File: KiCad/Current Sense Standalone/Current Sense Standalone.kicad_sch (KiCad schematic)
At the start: 11 parts, among them J1 PLUG INPUT BATTERY IN HERE (X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, J3 V+/- TEST Header PIN, J4 BAT +TERMINAL TEST HEADER PIN, J5 HEADER PIN FOR TEST, J6 to MCU GPIO PIN, J7 PLUG BATTERY OUTPUT HERE (XT6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, U1 INA139QPWRQ1

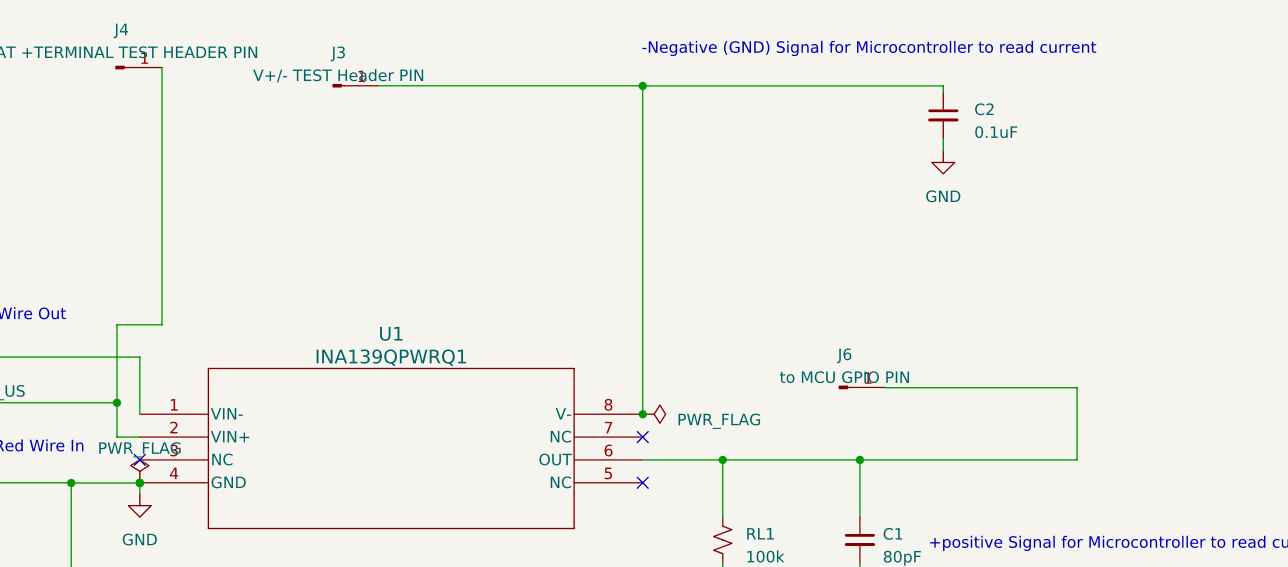
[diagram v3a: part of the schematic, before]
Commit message: Current Sense Update
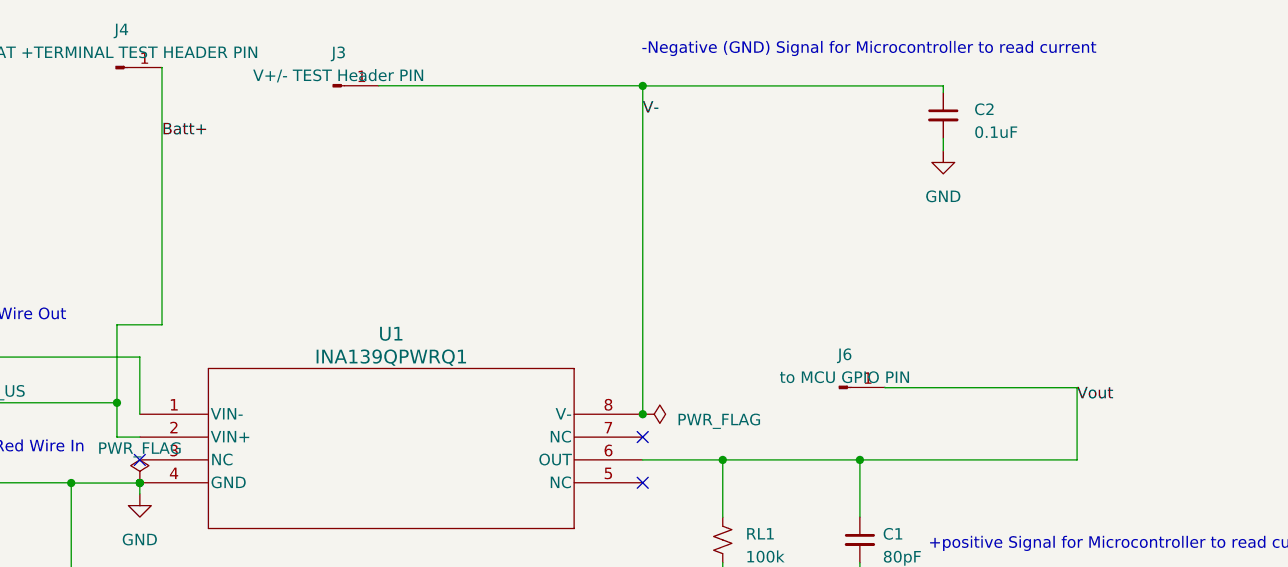
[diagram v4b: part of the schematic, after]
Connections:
- net V-: now reaches C2.1, J3.1 (Pin_1), U1.8 (V-)
- net Vout: now reaches C1.1, J6.1 (Pin_1), RL1.1, U1.6 (OUT)
- net Batt+: now reaches J1.1 (Pin_1), J4.1 (Pin_1), Rs1.2, U1.2 (VIN+)
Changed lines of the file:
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@@
+    (effects (font (size 1.27 1.27)) (justify left bottom))
+  )
+  (label "Vout" (at 250.19 85.09 0) (fields_autoplaced)
+    (effects (font (size 1.27 1.27)) (justify left bottom))
+  )
+  (label "Batt+" (at 148.5138 55.755 0) (fields_autoplaced)
+    (effects (font (size 1.27 1.27)) (justify left bottom))
+  )
+  (label "V-" (at 201.93 53.34 0) (fields_autoplaced)
     (effects (font (size 1.27 1.27)) (justify left bottom))
   )

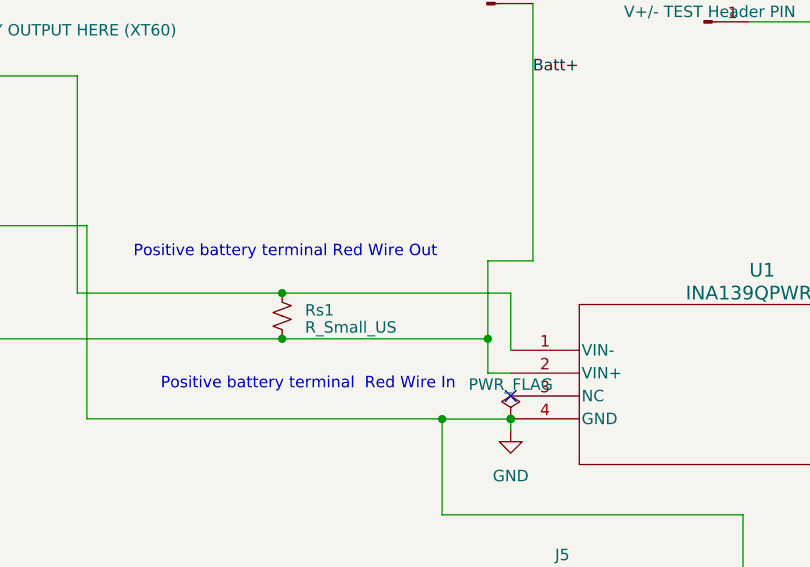
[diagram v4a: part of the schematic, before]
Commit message: Current Sense Update
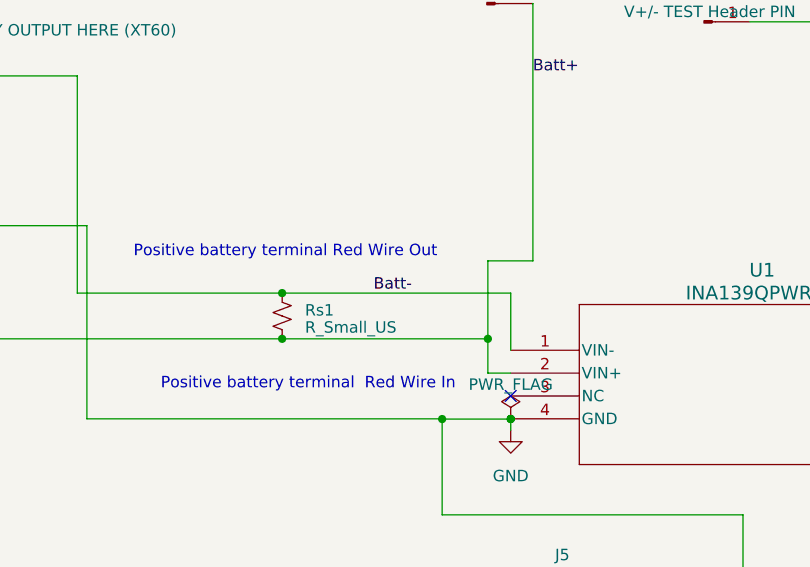
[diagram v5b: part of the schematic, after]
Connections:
- net Batt-: now reaches J7.1 (Pin_1), Rs1.1, U1.1 (VIN-)
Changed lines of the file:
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@@
+    (effects (font (size 1.27 1.27)) (justify left bottom))
+  )
+  (label "Batt-" (at 130.81 80.01 0) (fields_autoplaced)
     (effects (font (size 1.27 1.27)) (justify left bottom))
   )

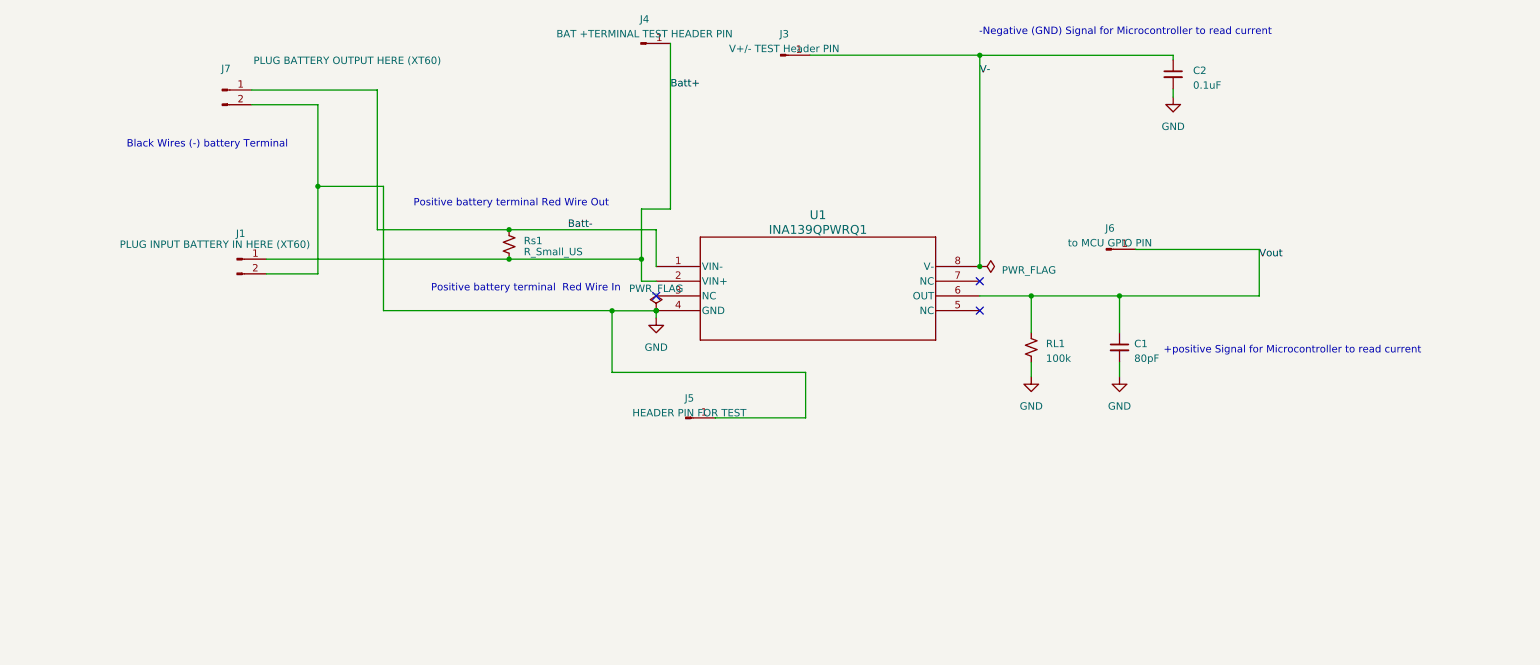
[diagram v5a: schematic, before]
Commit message: Updated Current Sense Standalone
new footprint for R_SENSE and fixed header pins
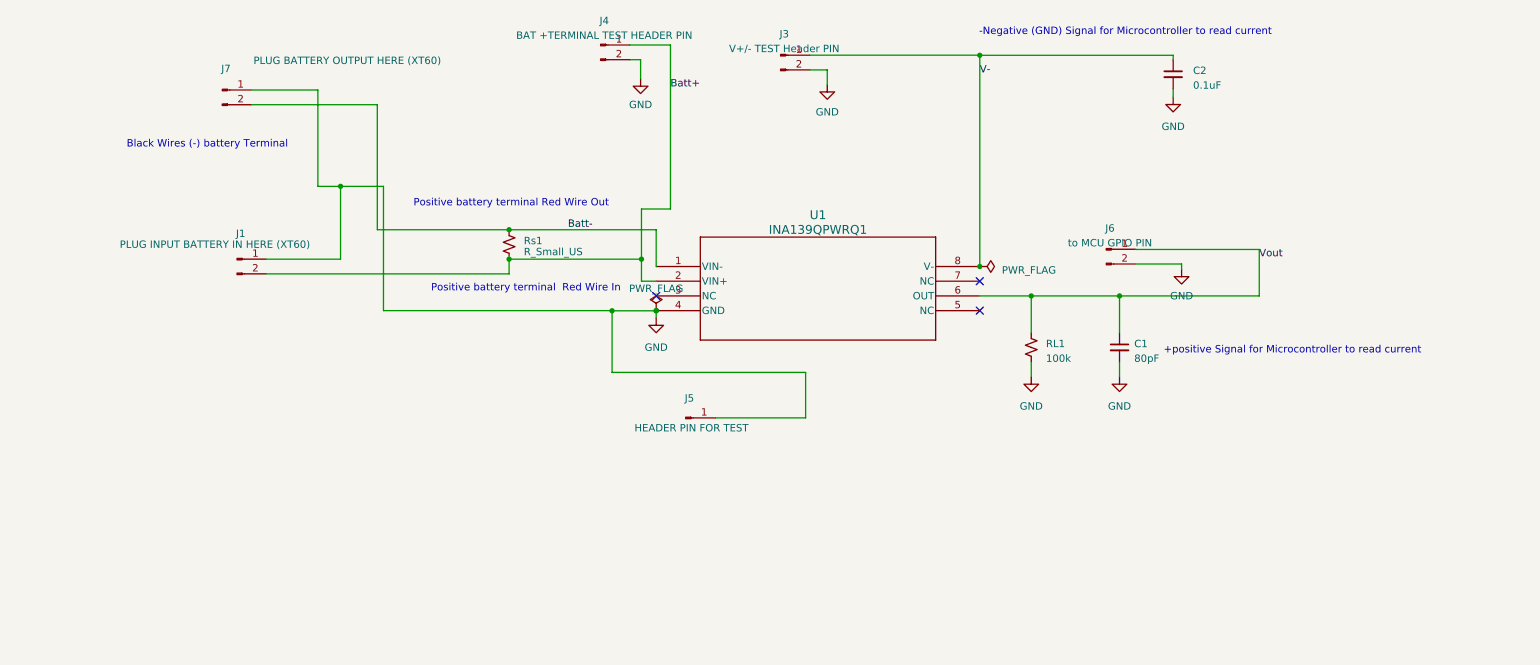
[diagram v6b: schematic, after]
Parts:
- J3, J4, J6: symbol Connector:Conn_01x01_Pin -> Connector:Conn_01x02_Pin
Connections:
- net Batt+: now also J1.2 (Pin_2); no longer J1.1 (Pin_1)
- net Batt-: now also J7.2 (Pin_2); no longer J7.1 (Pin_1)
- net GND: now also J1.1 (Pin_1), J3.2 (Pin_2), J4.2 (Pin_2), J6.2 (Pin_2), J7.1 (Pin_1); no longer J1.2 (Pin_2), J7.2 (Pin_2)
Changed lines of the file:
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@@
   (junction (at 120.65 80.01) (diameter 0) (color 0 0 0 0)
   )
-  (junction (at 120.65 85.09) (diameter 0) (color 0 0 0 0)
-  )
-  (junction (at 87.63 72.517) (diameter 0) (color 0 0 0 0)
-  )
   (junction (at 146.05 94.006) (diameter 0) (color 0 0 0 0)
   )
@@
   (junction (at 226.06 91.44) (diameter 0) (color 0 0 0 0)
   )
+  (junction (at 91.5454 72.517) (diameter 0) (color 0 0 0 0)
+  )
   (junction (at 201.93 86.36) (diameter 0) (color 0 0 0 0)
   )
+  (junction (at 120.65 85.09) (diameter 0) (color 0 0 0 0)
+  )
   (junction (at 210.82 91.44) (diameter 0) (color 0 0 0 0)
   )
@@
   (no_connect (at 201.93 88.9))
   (no_connect (at 201.93 93.98))
-  (wire (pts (xy 78.74 87.63) (xy 87.63 87.63))
-    (stroke (width 0) (type default))
-  )
   (wire (pts (xy 146.05 80.01) (xy 146.05 86.36))
     (stroke (width 0) (type default))
@@
     (stroke (width 0) (type default))
   )
-  (wire (pts (xy 87.63 72.517) (xy 87.63 87.63))
-    (stroke (width 0) (type default))
-  )
   (wire (pts (xy 138.43 93.98) (xy 138.43 94.006))
     (stroke (width 0) (type default))
@@
     (stroke (width 0) (type default))
   )
-  (wire (pts (xy 97.8916 80.01) (xy 97.8916 55.88))
-    (stroke (width 0) (type default))
-  )
-  (wire (pts (xy 87.63 58.42) (xy 87.63 72.517))
-    (stroke (width 0) (type default))
-  )
   (wire (pts (xy 156.2293 112.505) (xy 156.2293 112.4966))
     (stroke (width 0) (type default))
@@
     (stroke (width 0) (type default))
   )
-  (wire (pts (xy 87.63 72.517) (xy 98.9584 72.517))
-    (stroke (width 0) (type default))
-  )
   (wire (pts (xy 156.2293 112.4966) (xy 171.8564 112.4966))
     (stroke (width 0) (type default))
@@
     (stroke (width 0) (type default))
   )
-  (wire (pts (xy 97.8916 55.88) (xy 76.2 55.88))
+  (wire (pts (xy 201.93 49.8856) (xy 235.3257 49.8856))
     (stroke (width 0) (type default))
   )
-  (wire (pts (xy 201.93 49.8856) (xy 235.3257 49.8856))
+  (wire (pts (xy 78.74 85.09) (xy 91.5454 85.09))
+    (stroke (width 0) (type default))
+  )
+  (wire (pts (xy 76.2 55.88) (xy 87.63 55.88))
     (stroke (width 0) (type default))
   )
@@
     (stroke (width 0) (type default))
   )
+  (wire (pts (xy 236.7788 85.9252) (xy 236.7788 86.8426))
+    (stroke (width 0) (type default))
+  )
+  (wire (pts (xy 141.5288 50.6476) (xy 143.3576 50.6476))
+    (stroke (width 0) (type default))
+  )
   (wire (pts (xy 146.05 95.25) (xy 146.05 94.006))
     (stroke (width 0) (type default))
@@
     (stroke (width 0) (type default))
   )
-  (wire (pts (xy 76.2 58.42) (xy 87.63 58.42))
+  (wire (pts (xy 91.5454 72.517) (xy 98.9584 72.517))
+    (stroke (width 0) (type default))
+  )
+  (wire (pts (xy 87.63 55.88) (xy 87.63 72.517))
+    (stroke (width 0) (type default))
+  )
+  (wire (pts (xy 228.8553 85.9252) (xy 236.7788 85.9252))
+    (stroke (width 0) (type default))
+  )
+  (wire (pts (xy 120.65 87.63) (xy 120.65 85.09))
+    (stroke (width 0) (type default))
+  )
+  (wire (pts (xy 143.3576 50.6476) (xy 143.3576 53.9496))
     (stroke (width 0) (type default))
   )
-  (wire (pts (xy 78.74 85.09) (xy 120.65 85.09))
+  (wire (pts (xy 87.63 72.517) (xy 91.5454 72.517))
     (stroke (width 0) (type default))
   )
@@
     (stroke (width 0) (type default))
   )
-  (wire (pts (xy 148.5138 76.4286) (xy 148.5138 47.842))
+  (wire (pts (xy 148.5138 76.4286) (xy 148.5138 48.1076))
     (stroke (width 0) (type default))
   )
@@
     (stroke (width 0) (type default))
   )
+  (wire (pts (xy 91.5454 85.09) (xy 91.5454 72.517))
+    (stroke (width 0) (type default))
+  )
   (wire (pts (xy 201.93 91.44) (xy 210.82 91.44))
     (stroke (width 0) (type default))
   )
-  (wire (pts (xy 148.5138 47.842) (xy 148.4828 47.842))
+  (wire (pts (xy 148.5138 48.1076) (xy 141.5288 48.1076))
     (stroke (width 0) (type default))
   )
@@
     (stroke (width 0) (type default))
   )
+  (wire (pts (xy 175.5902 52.4073) (xy 175.5902 54.9402))
+    (stroke (width 0) (type default))
+  )
   (wire (pts (xy 210.82 91.44) (xy 226.06 91.44))
     (stroke (width 0) (type default))
@@
     (stroke (width 0) (type default))
   )
+  (wire (pts (xy 97.8916 58.42) (xy 97.8916 80.01))
+    (stroke (width 0) (type default))
+  )
   (wire (pts (xy 143.51 85.09) (xy 143.51 88.9))
     (stroke (width 0) (type default))
@@
     (stroke (width 0) (type default))
   )
+  (wire (pts (xy 78.74 87.63) (xy 120.65 87.63))
+    (stroke (width 0) (type default))
+  )
+  (wire (pts (xy 76.2 58.42) (xy 97.8916 58.42))
+    (stroke (width 0) (type default))
+  )
   (wire (pts (xy 148.5138 76.4286) (xy 143.51 76.4286))
     (stroke (width 0) (type default))
@@
     (stroke (width 0) (type default))
   )
+  (wire (pts (xy 172.6111 52.4073) (xy 175.5902 52.4073))
+    (stroke (width 0) (type default))
+  )
   (wire (pts (xy 235.3257 50.6164) (xy 235.3257 49.8856))
     (stroke (width 0) (type default))
@@
     (effects (font (size 1.27 1.27)) (justify left bottom))
   )
-  (symbol (lib_id "Connector:Conn_01x01_Pin") (at 167.5311 49.8673 0) (unit 1)
+  (symbol (lib_id "Connector:Conn_01x02_Pin") (at 167.5311 49.8673 0) (unit 1)
     (in_bom yes) (on_board yes) (dnp no) (fields_autoplaced)
     (property "Reference" "J3" (at 168.1661 46.2097 0)
@@
     )
     (pin "1")
+    (pin "2")
     (instances
       (project "Current Sense Standalone"
@@
     )
   )
-  (symbol (lib_id "Connector:Conn_01x01_Pin") (at 223.7753 83.3852 0) (unit 1)
+  (symbol (lib_id "Connector:Conn_01x02_Pin") (at 223.7753 83.3852 0) (unit 1)
     (in_bom yes) (on_board yes) (dnp no) (fields_autoplaced)
     (property "Reference" "J6" (at 224.4103 79.753 0)
@@
     )
     (pin "1")
+    (pin "2")
     (instances
       (project "Current Sense Standalone"
@@
     )
   )
+  (symbol (lib_id "power:GND") (at 175.5902 54.9402 0) (unit 1)
+    (in_bom yes) (on_board yes) (dnp no) (fields_autoplaced)
+    (property "Reference" "#PWR06" (at 175.5902 61.2902 0)
+      (effects (font (size 1.27 1.27)) hide)
+    )
+    (property "Value" "GND" (at 175.5902 59.69 0)
+      (effects (font (size 1.27 1.27)))
+    )
+    (property "Footprint" "" (at 175.5902 54.9402 0)
+      (effects (font (size 1.27 1.27)) hide)
+    )
+    (property "Datasheet" "" (at 175.5902 54.9402 0)
+      (effects (font (size 1.27 1.27)) hide)
+    )
+    (pin "1")
+    (instances
+      (project "Current Sense Standalone"
+        (path "/af3dddb2-191c-40a1-9395-0fad50eefcf8"
+          (reference "#PWR06") (unit 1)
+        )
+      )
+    )
+  )
   (symbol (lib_id "power:GND") (at 146.05 95.25 0) (unit 1)
     (in_bom yes) (on_board yes) (dnp no) (fields_autoplaced)
@@
   )
   (symbol (lib_id "Connector:Conn_01x01_Pin") (at 151.1493 112.505 0) (unit 1)
-    (in_bom yes) (on_board yes) (dnp no) (fields_autoplaced)
+    (in_bom yes) (on_board yes) (dnp no)
     (property "Reference" "J5" (at 151.7843 109.1014 0)
       (effects (font (size 1.27 1.27)))
     )
-    (property "Value" "HEADER PIN FOR TEST" (at 151.7843 111.6414 0)
+    (property "Value" "HEADER PIN FOR TEST" (at 152.146 114.2492 0)
       (effects (font (size 1.27 1.27)))
     )
@@
     )
   )
-  (symbol (lib_id "Connector:Conn_01x01_Pin") (at 143.4028 47.842 0) (unit 1)
+  (symbol (lib_id "Connector:Conn_01x02_Pin") (at 136.4488 48.1076 0) (unit 1)
     (in_bom yes) (on_board yes) (dnp no) (fields_autoplaced)
-    (property "Reference" "J4" (at 144.0378 43.651 0)
+    (property "Reference" "J4" (at 137.0838 43.9166 0)
       (effects (font (size 1.27 1.27)))
     )
-    (property "Value" "BAT +TERMINAL TEST HEADER PIN" (at 144.0378 46.191 0)
+    (property "Value" "BAT +TERMINAL TEST HEADER PIN" (at 137.0838 46.4566 0)
       (effects (font (size 1.27 1.27)))
     )
-    (property "Footprint" "Connector_PinHeader_2.54mm:PinHeader_1x02_P2.54mm_Vertical" (at 143.4028 47.842 0)
+    (property "Footprint" "Connector_PinHeader_2.54mm:PinHeader_1x02_P2.54mm_Vertical" (at 136.4488 48.1076 0)
       (effects (font (size 1.27 1.27)) hide)
     )
-    (property "Datasheet" "~" (at 143.4028 47.842 0)
+    (property "Datasheet" "~" (at 136.4488 48.1076 0)
       (effects (font (size 1.27 1.27)) hide)
     )
     (pin "1")
+    (pin "2")
     (instances
       (project "Current Sense Standalone"
@@
         )
       )
+    )
+  )
+  (symbol (lib_id "power:GND") (at 236.7788 86.8426 0) (unit 1)
+    (in_bom yes) (on_board yes) (dnp no) (fields_autoplaced)
+    (property "Reference" "#PWR07" (at 236.7788 93.1926 0)
+      (effects (font (size 1.27 1.27)) hide)
+    )
+    (property "Value" "GND" (at 236.7788 91.44 0)
+      (effects (font (size 1.27 1.27)))
+    )
+    (property "Footprint" "" (at 236.7788 86.8426 0)
+      (effects (font (size 1.27 1.27)) hide)
+    )
+    (property "Datasheet" "" (at 236.7788 86.8426 0)
+      (effects (font (size 1.27 1.27)) hide)
+    )
+    (pin "1")
+    (instances
+      (project "Current Sense Standalone"
+        (path "/af3dddb2-191c-40a1-9395-0fad50eefcf8"
+          (reference "#PWR07") (unit 1)
+        )
+      )
+    )
+  )
+  (symbol (lib_id "power:GND") (at 143.3576 53.9496 0) (unit 1)
+    (in_bom yes) (on_board yes) (dnp no) (fields_autoplaced)
+    (property "Reference" "#PWR04" (at 143.3576 60.2996 0)
+      (effects (font (size 1.27 1.27)) hide)
+    )
+    (property "Value" "GND" (at 143.3576 58.42 0)
+      (effects (font (size 1.27 1.27)))
+    )
+    (property "Footprint" "" (at 143.3576 53.9496 0)
+      (effects (font (size 1.27 1.27)) hide)
+    )
+    (property "Datasheet" "" (at 143.3576 53.9496 0)
+      (effects (font (size 1.27 1.27)) hide)
+    )
+    (pin "1")
+    (instances
+      (project "Current Sense Standalone"
+        (path "/af3dddb2-191c-40a1-9395-0fad50eefcf8"
+          (reference "#PWR04") (unit 1)
+        )
+      )
